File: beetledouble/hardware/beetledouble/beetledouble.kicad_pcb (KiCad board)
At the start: 4 copper layers, 32 x 60 mm, 63 parts, among them J1 XT30PW-M, J2 rxin, J4 motor_out, J5 motor_out, J6 prog connector, Q1 SE3082G, Q2 SE3082G, Q3 SE3082G, Q4 SE3082G, U1 78L12G-AB3-R, U2 DD4012SB, U3 ATtiny1614-SS, U4 NCP81155MN, U5 NCP81155MN, U6 NCP81155MN, U7 NCP81155MN

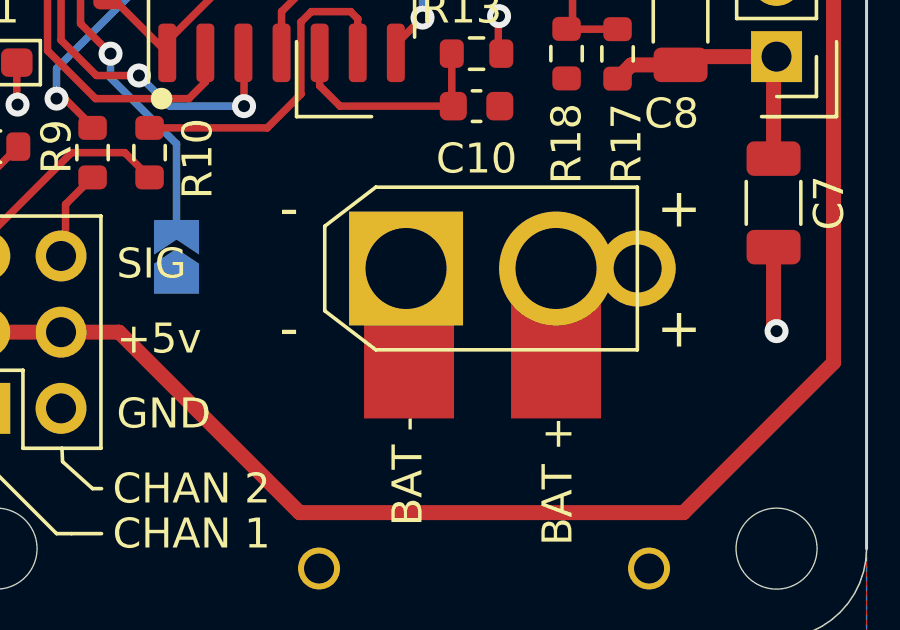
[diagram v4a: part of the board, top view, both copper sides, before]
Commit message: Power connector update etc
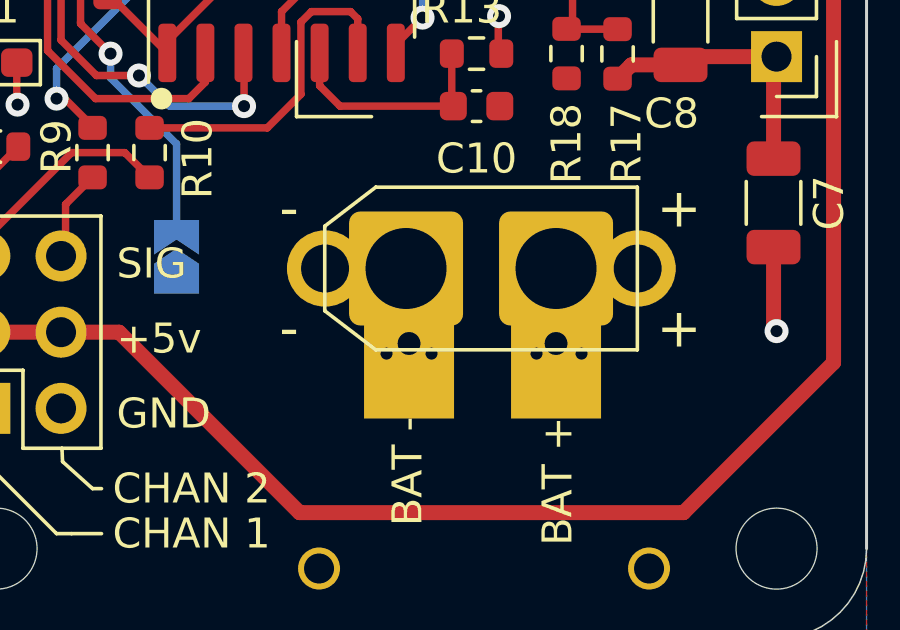
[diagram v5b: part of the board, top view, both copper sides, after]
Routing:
- net VBAT: vias 17 -> 19
- net GND: vias 7 -> 9
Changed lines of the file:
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@@
+      (effects (font (size 1.3 1.3) (thickness 0.15)))
+    )
+    (fp_text user "-" (at -4 2 unlocked) (layer "F.SilkS")
       (effects (font (size 1.3 1.3) (thickness 0.15)))
     )
@@
       (effects (font (size 1.3 1.3) (thickness 0.15)))
     )
-    (fp_text user "-" (at -4 2 unlocked) (layer "F.SilkS")
-      (effects (font (size 1.3 1.3) (thickness 0.15)))
-    )
     (fp_text user "-" (at -4 -2 unlocked) (layer "F.SilkS")
       (effects (font (size 1.3 1.3) (thickness 0.15)))
     )
+    (fp_line (start -2.81 -1.41) (end -2.81 1.41) (layer "F.SilkS") (width 0.12))
+    (fp_line (start -1.11 2.71) (end 7.61 2.71) (layer "F.SilkS") (width 0.12))
     (fp_line (start -2.81 -1.41) (end -1.11 -2.71) (layer "F.SilkS") (width 0.12))
-    (fp_line (start -1.11 2.71) (end 7.61 2.71) (layer "F.SilkS") (width 0.12))
-    (fp_line (start -2.81 -1.41) (end -2.81 1.41) (layer "F.SilkS") (width 0.12))
+    (fp_line (start 7.61 -2.71) (end 7.61 2.71) (layer "F.SilkS") (width 0.12))
     (fp_line (start -1.11 -2.71) (end 7.61 -2.71) (layer "F.SilkS") (width 0.12))
     (fp_line (start -2.81 1.41) (end -1.11 2.71) (layer "F.SilkS") (width 0.12))
-    (fp_line (start 7.61 -2.71) (end 7.61 2.71) (layer "F.SilkS") (width 0.12))
-    (fp_line (start -5.72 5) (end -5.72 -4.5) (layer "F.CrtYd") (width 0.05))
-    (fp_line (start -5.72 -4.5) (end 10.5 -4.5) (layer "F.CrtYd") (width 0.05))
     (fp_line (start 10.5 -4.5) (end 10.5 5) (layer "F.CrtYd") (width 0.05))
     (fp_line (start 10.5 5) (end -5.72 5) (layer "F.CrtYd") (width 0.05))
+    (fp_line (start -5.72 -4.5) (end 10.5 -4.5) (layer "F.CrtYd") (width 0.05))
+    (fp_line (start -5.72 5) (end -5.72 -4.5) (layer "F.CrtYd") (width 0.05))
+    (fp_line (start -2.7 -1.3) (end -1 -2.6) (layer "F.Fab") (width 0.1))
+    (fp_line (start -1 -2.6) (end 7.5 -2.6) (layer "F.Fab") (width 0.1))
+    (fp_line (start 7.5 -2.6) (end 7.5 2.6) (layer "F.Fab") (width 0.1))
+    (fp_line (start -1 2.6) (end 7.5 2.6) (layer "F.Fab") (width 0.1))
     (fp_line (start -2.7 1.3) (end -1 2.6) (layer "F.Fab") (width 0.1))
-    (fp_line (start 7.5 -2.6) (end 7.5 2.6) (layer "F.Fab") (width 0.1))
     (fp_line (start -2.7 -1.3) (end -2.7 1.3) (layer "F.Fab") (width 0.1))
-    (fp_line (start -2.7 -1.3) (end -1 -2.6) (layer "F.Fab") (width 0.1))
-    (fp_line (start -1 2.6) (end 7.5 2.6) (layer "F.Fab") (width 0.1))
-    (fp_line (start -1 -2.6) (end 7.5 -2.6) (layer "F.Fab") (width 0.1))
     (pad "" thru_hole circle locked (at -3 10) (size 1.4 1.4) (drill 1) (layers *.Cu *.Mask))
     (pad "" thru_hole circle locked (at 8 10) (size 1.4 1.4) (drill 1) (layers *.Cu *.Mask))
-    (pad "1" thru_hole rect locked (at -0.1 0) (size 3.8 3.8) (drill 2.7) (layers *.Cu *.Mask)
-      (net 2 "GND") (pinfunction "Pin_1") (pintype "passive"))
-    (pad "1" smd rect (at 0 2.5) (size 3 5) (layers "F.Cu" "F.Mask")
-      (net 2 "GND") (pinfunction "Pin_1") (pintype "passive"))
-    (pad "2" smd rect (at 4.9 2.5) (size 3 5) (layers "F.Cu" "F.Mask")
-      (net 3 "VBAT") (pinfunction "Pin_2") (pintype "passive"))
+    (pad "1" thru_hole rect (at 0 2.5) (size 3 5) (drill 0.762) (layers *.Cu *.Mask) (remove_unused_layers) (keep_end_layers)
+      (net 2 "GND") (pinfunction "Pin_1"))
+    (pad "1" thru_hole circle locked (at -2.8 0) (size 2.54 2.54) (drill 1.6) (layers *.Cu *.Mask)
+      (net 2 "GND") (pinfunction "Pin_1"))
+    (pad "1" thru_hole roundrect locked (at -0.1 0) (size 3.8 3.8) (drill 2.7) (layers *.Cu *.Mask) (roundrect_rratio 0.1)
+      (net 2 "GND") (pinfunction "Pin_1"))
+    (pad "2" thru_hole roundrect locked (at 4.9 0) (size 3.8 3.8) (drill 2.7) (layers *.Cu *.Mask) (roundrect_rratio 0.1)
+      (net 3 "VBAT") (pinfunction "Pin_2"))
+    (pad "2" thru_hole rect (at 4.9 2.5) (size 3 5) (drill 0.762) (layers *.Cu *.Mask) (remove_unused_layers) (keep_end_layers)
+      (net 3 "VBAT") (pinfunction "Pin_2"))
     (pad "2" thru_hole circle locked (at 7.62 0) (size 2.54 2.54) (drill 1.6) (layers *.Cu *.Mask)
-      (net 3 "VBAT") (pinfunction "Pin_2") (pintype "passive"))
-    (pad "2" thru_hole circle locked (at 4.9 0) (size 3.8 3.8) (drill 2.7) (layers *.Cu *.Mask)
-      (net 3 "VBAT") (pinfunction "Pin_2") (pintype "passive"))
+      (net 3 "VBAT") (pinfunction "Pin_2"))
   )
   (footprint "Resistor_SMD:R_0603_1608Metric" (layer "F.Cu")
@@
   (via (at 129.75 101.5) (size 0.8) (drill 0.4) (layers "F.Cu" "B.Cu") (net 2))
   (via (at 123.962247 100.087649) (size 0.8) (drill 0.4) (layers "F.Cu" "B.Cu") (net 2))
+  (via (at 123 121.5) (size 0.8) (drill 0.4) (layers "F.Cu" "B.Cu") (net 2))
+  (via (at 121.5 121.5) (size 0.8) (drill 0.4) (layers "F.Cu" "B.Cu") (net 2))
   (segment (start 134.4 111.9675) (end 134.6175 111.75) (width 0.5) (layer "F.Cu") (net 3))
   (segment (start 134.5 111.6) (end 131.575 111.6) (width 0.5) (layer "F.Cu") (net 3))
@@
   (via (at 122 80.5) (size 0.8) (drill 0.4) (layers "F.Cu" "B.Cu") (free) (net 3))
   (via (at 121 80.5) (size 0.8) (drill 0.4) (layers "F.Cu" "B.Cu") (free) (net 3))
+  (via (at 126.5 121.5) (size 0.8) (drill 0.4) (layers "F.Cu" "B.Cu") (net 3))
   (via (at 115 81.5) (size 0.8) (drill 0.4) (layers "F.Cu" "B.Cu") (free) (net 3))
   (via (at 130 80.5) (size 0.8) (drill 0.4) (layers "F.Cu" "B.Cu") (free) (net 3))
@@
   (via (at 129 81.5) (size 0.8) (drill 0.4) (layers "F.Cu" "B.Cu") (free) (net 3))
   (via (at 108 80.5) (size 0.8) (drill 0.4) (layers "F.Cu" "B.Cu") (free) (net 3))
+  (via (at 128 121.5) (size 0.8) (drill 0.4) (layers "F.Cu" "B.Cu") (net 3))
   (via (at 114 81.5) (size 0.8) (drill 0.4) (layers "F.Cu" "B.Cu") (free) (net 3))
   (segment (start 106.57548 108.07952) (end 106.75 107.905) (width 0.25) (layer "F.Cu") (net 4))
@@
     )
   )
-  (zone (net 0) (net_name "") (layer "F.Cu") (hatch edge 0.508)
+  (zone (net 0) (net_name "") (layers F&B.Cu) (name "soldering-allow") (hatch edge 0.508)
     (connect_pads yes (clearance 0))
     (min_thickness 0.254)
@@
     (polygon
       (pts
-        (xy 130.5 129)
-        (xy 119.5 129)
-        (xy 119.5 120.5)
-        (xy 130.5 120.5)
+        (xy 132 117.5)
+        (xy 132 122.5)
+        (xy 131 123.5)
+        (xy 130 124.5)
+        (xy 124.5 124.5)
+        (xy 124.5 116)
+        (xy 130.5 116)
+        (xy 131.5 117)
       )
     )
@@
       )
     )
-  )
-  (zone (net 0) (net_name "") (layers "In1.Cu" "In2.Cu") (name "no-vbat") (hatch edge 0.508)
-    (connect_pads (clearance 0))
-    (min_thickness 0.254)
-    (keepout (tracks allowed) (vias allowed) (pads allowed ) (copperpour not_allowed) (footprints allowed))
-    (fill (thermal_gap 0.508) (thermal_bridge_width 0.508))
-    (polygon
-      (pts
-        (xy 124.5 126)
-        (xy 119.5 126)
-        (xy 119.5 115.5)
-        (xy 124.5 115.5)
-      )
-    )

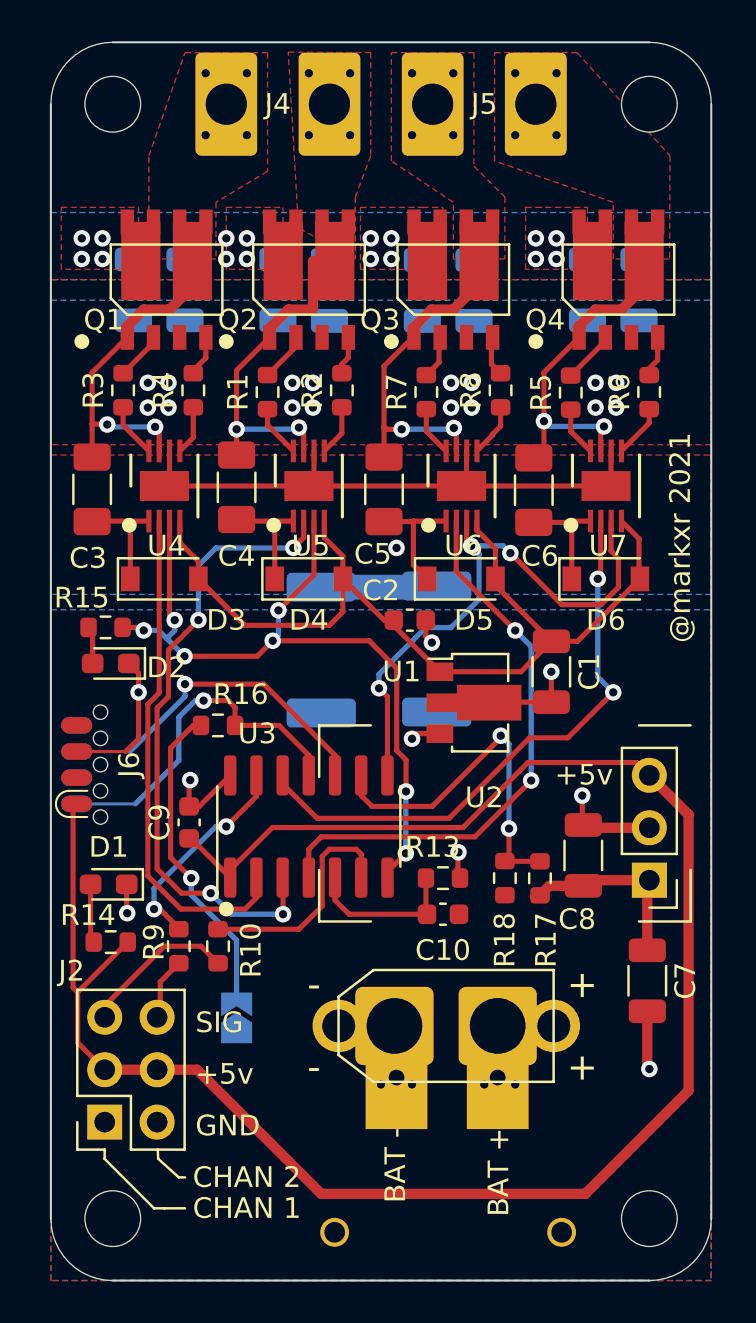
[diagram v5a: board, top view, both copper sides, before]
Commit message: slightly shrink
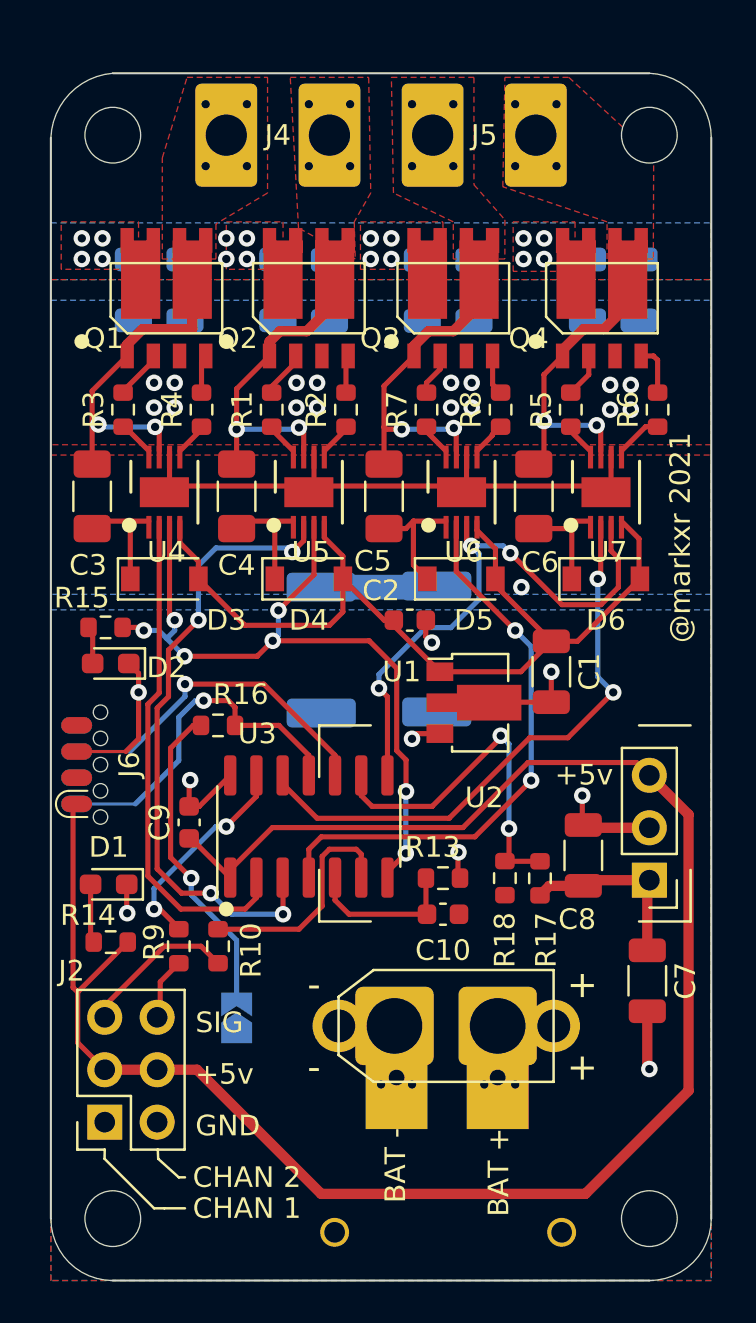
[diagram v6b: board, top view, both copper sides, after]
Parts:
- moved H3 1.50 mm to (134.5, 75.5)
- moved H4 1.50 mm to (108.5, 75.5)
- moved J4 1.50 mm to (114.0, 75.5)
- moved J5 1.50 mm to (124.0, 75.5)
- moved Q4 1.20 mm to (132.2, 83.4)
- moved R4 1.02 mm to (112.8, 88.8)
- moved R2 0.96 mm to (119.8, 88.8)
- moved R6 0.94 mm to (134.9, 88.8)
- moved R3 0.94 mm to (109.0, 88.8)
- moved R8 0.94 mm to (127.3, 88.8)
- moved Q1 0.90 mm to (111.1, 83.4)
- moved Q2 0.90 mm to (118.0, 83.4)
- moved Q3 0.90 mm to (125.0, 83.4)
- moved R1 0.87 mm to (116.2, 88.8)
- moved R7 0.85 mm to (123.7, 88.8)
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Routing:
- net /driver2/MOTORS2: track 16.8 -> 15.4 mm
- net /driver1/MOTORS1: track 15.5 -> 16.7 mm
- net /driver1/MOTORH2: track 2.54 -> 1.61 mm
- net /driver2/MOTORL1: track 2.59 -> 1.67 mm
- net /driver1/MOTORH1: track 2.63 -> 1.74 mm
- net /driver1/MOTORL2: track 2.46 -> 1.61 mm
- net /driver2/MOTORH1: track 2.42 -> 1.57 mm
- net /driver2/MOTORH2: track 2.39 -> 1.57 mm
- net /driver1/MOTORL1: track 2.38 -> 1.61 mm
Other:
- board size 32 x 60 mm -> 32 x 58.5 mm

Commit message: shrink board slightly
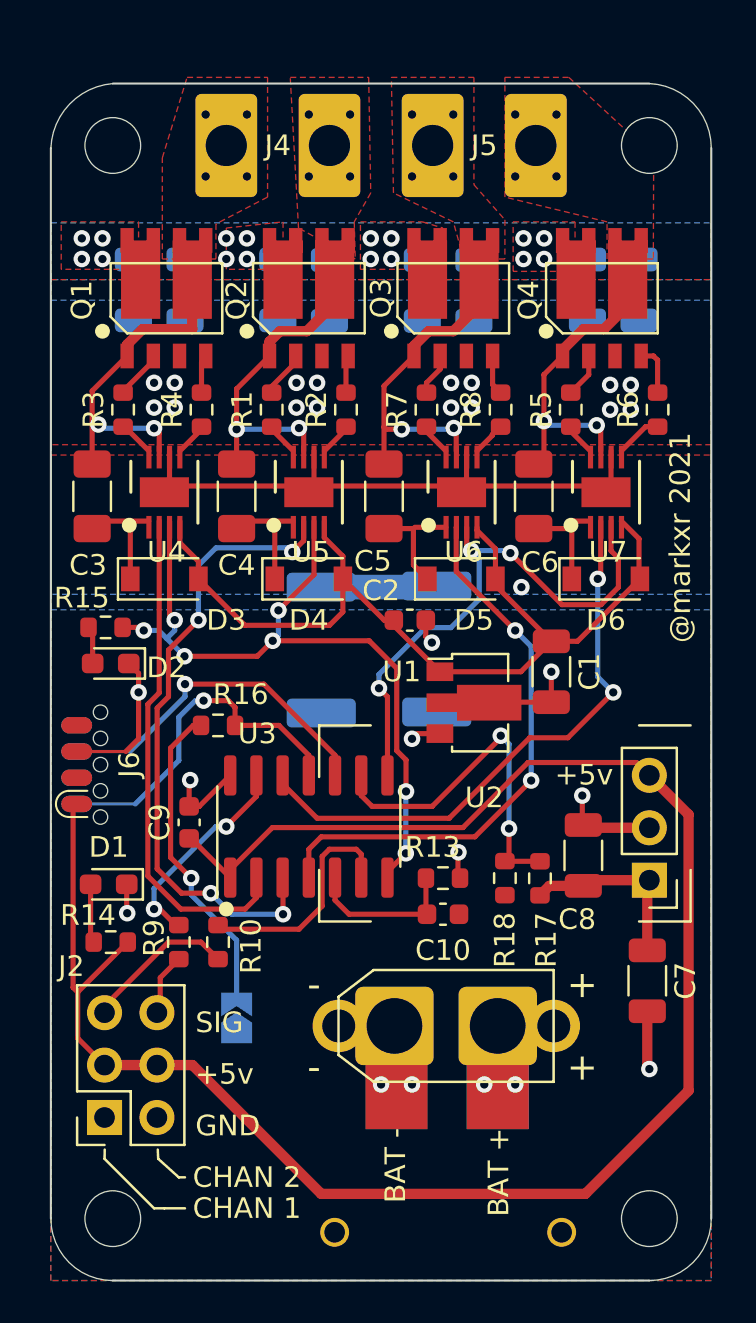
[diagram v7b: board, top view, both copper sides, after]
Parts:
- moved H3 0.50 mm to (134.5, 76.0)
- moved H4 0.50 mm to (108.5, 76.0)
- moved J4 0.50 mm to (114.0, 76.0)
- moved J5 0.50 mm to (124.0, 76.0)
- moved J2 0.23 mm to (108.1, 123.1)
- moved R10 0.20 mm to (113.6, 114.6)
- moved R9 0.20 mm to (111.7, 114.6)
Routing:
- net /driver2/BOOST1: track 6.23 -> 5.66 mm
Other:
- board size 32 x 58.5 mm -> 32 x 58 mm
